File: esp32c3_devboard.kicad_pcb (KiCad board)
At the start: 2 copper layers, 42 parts, among them J1 UART USB, J2 JTAG USB, J3 Conn_01x15_Male, J4 Conn_01x15_Male, SW1 SW_RSTN, SW2 SW_USR, U1 ESP32-C3-MINI-1, U2 SRV05-4, U3 AMS1117, U4 CP2102N-A01-GQFN28

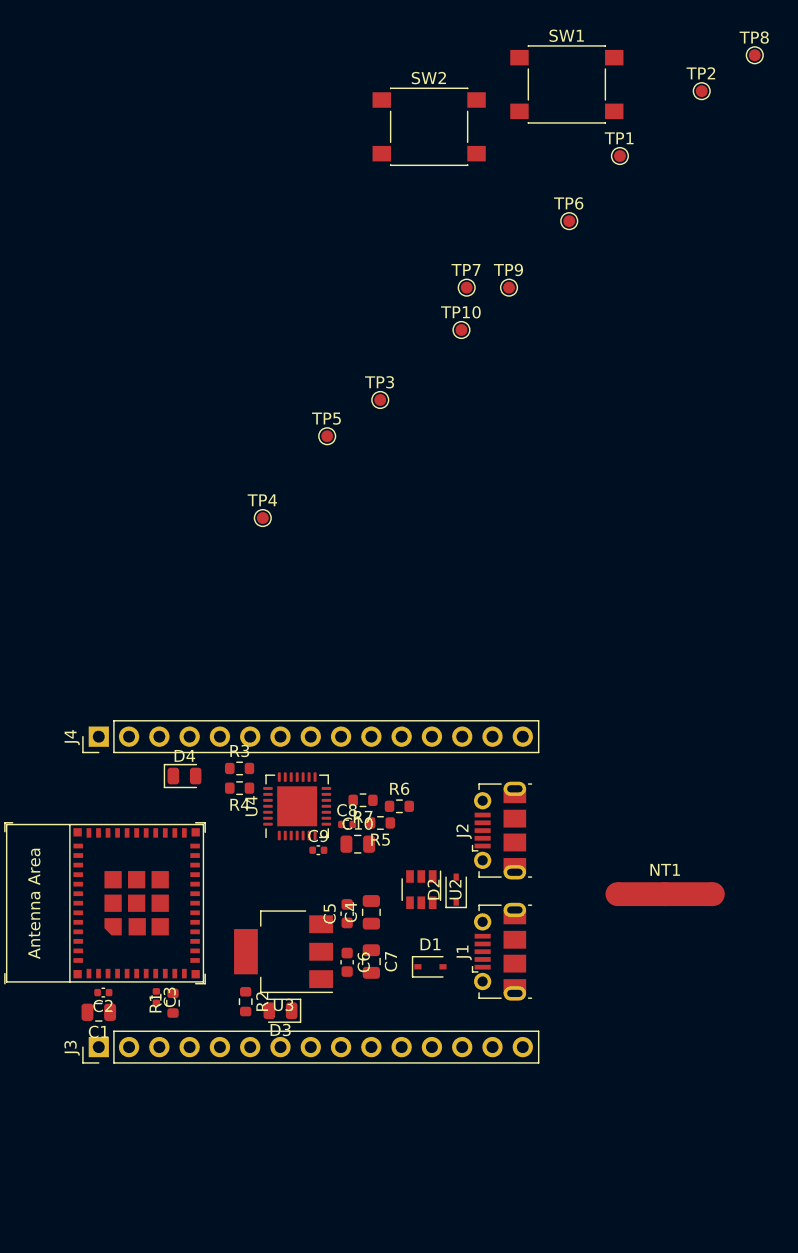
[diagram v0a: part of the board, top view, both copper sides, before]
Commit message: Add pullup on GPIO2 strapping pin
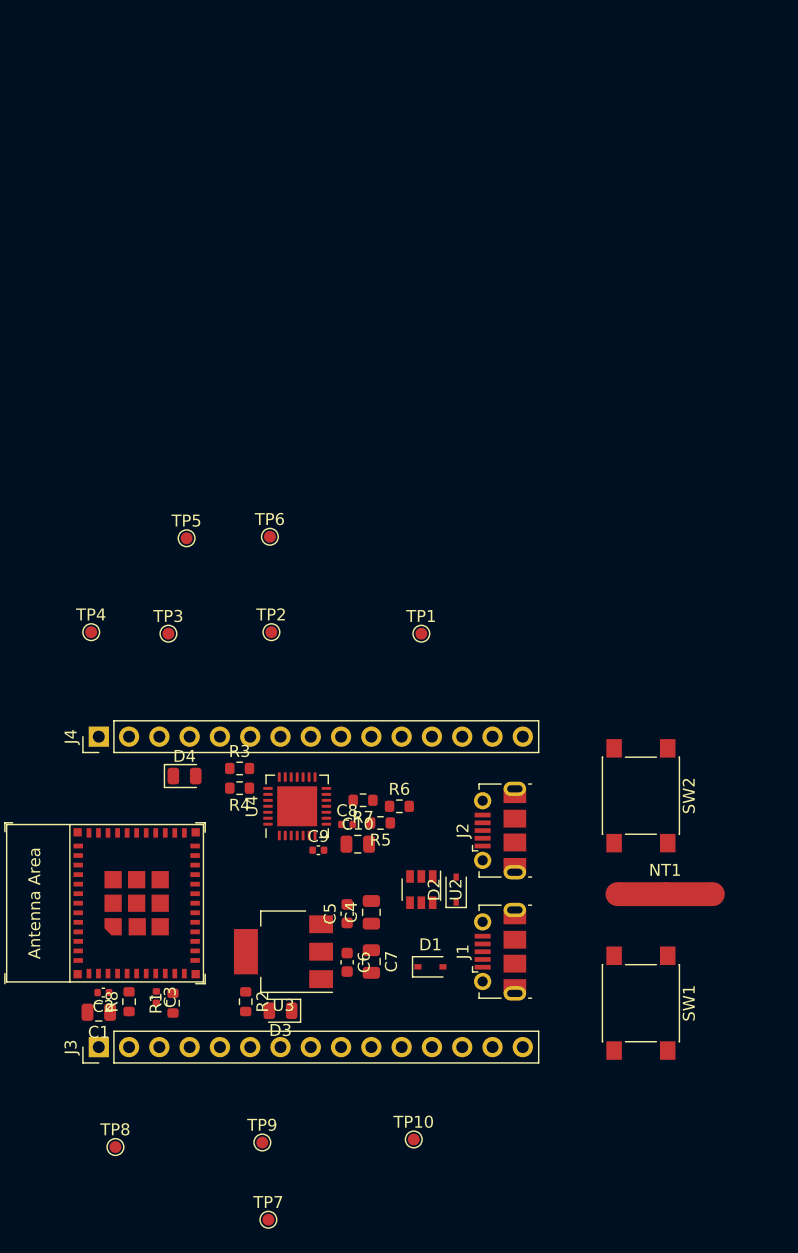
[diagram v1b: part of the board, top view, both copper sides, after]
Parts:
- added R8: 10K, Resistor_SMD:R_0603_1608Metric, F.Cu at (113.0, 149.2)
- moved TP8 106.1 mm to (111.9, 161.4)
- moved TP7 79.9 mm to (124.7, 167.5)
- moved SW1 77.3 mm to (156.0, 149.4), turned to 270 degrees
- moved TP9 74.6 mm to (124.2, 161.0)
- moved TP10 68.0 mm to (136.9, 160.8)
- moved SW2 58.8 mm to (156.0, 132.0), turned to 270 degrees
- moved TP2 58.0 mm to (125.0, 118.2)
- moved TP1 43.4 mm to (137.5, 118.4)
- moved TP6 36.5 mm to (124.8, 110.2)
- moved TP3 26.5 mm to (116.3, 118.4)
- moved TP4 17.3 mm to (109.9, 118.2)
- moved TP5 14.6 mm to (117.9, 110.4)

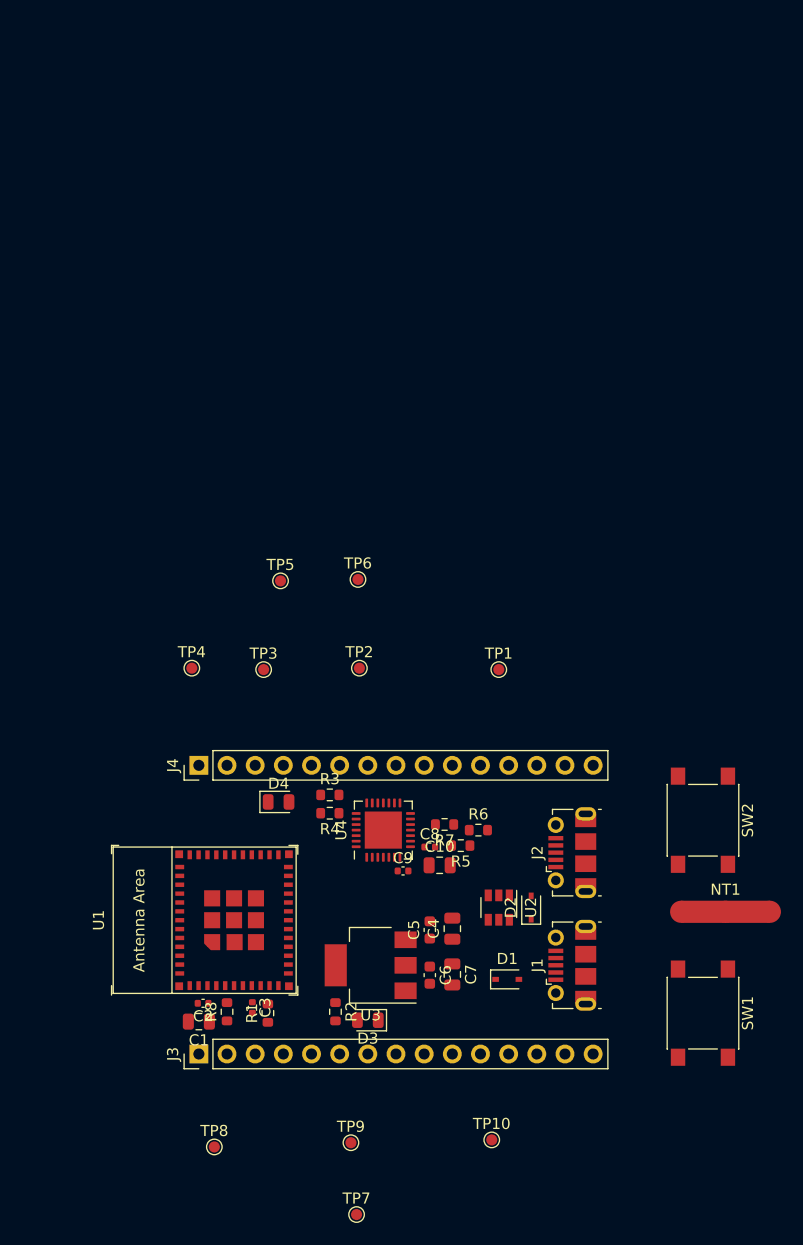
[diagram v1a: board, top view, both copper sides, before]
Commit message: Add micro USB step files
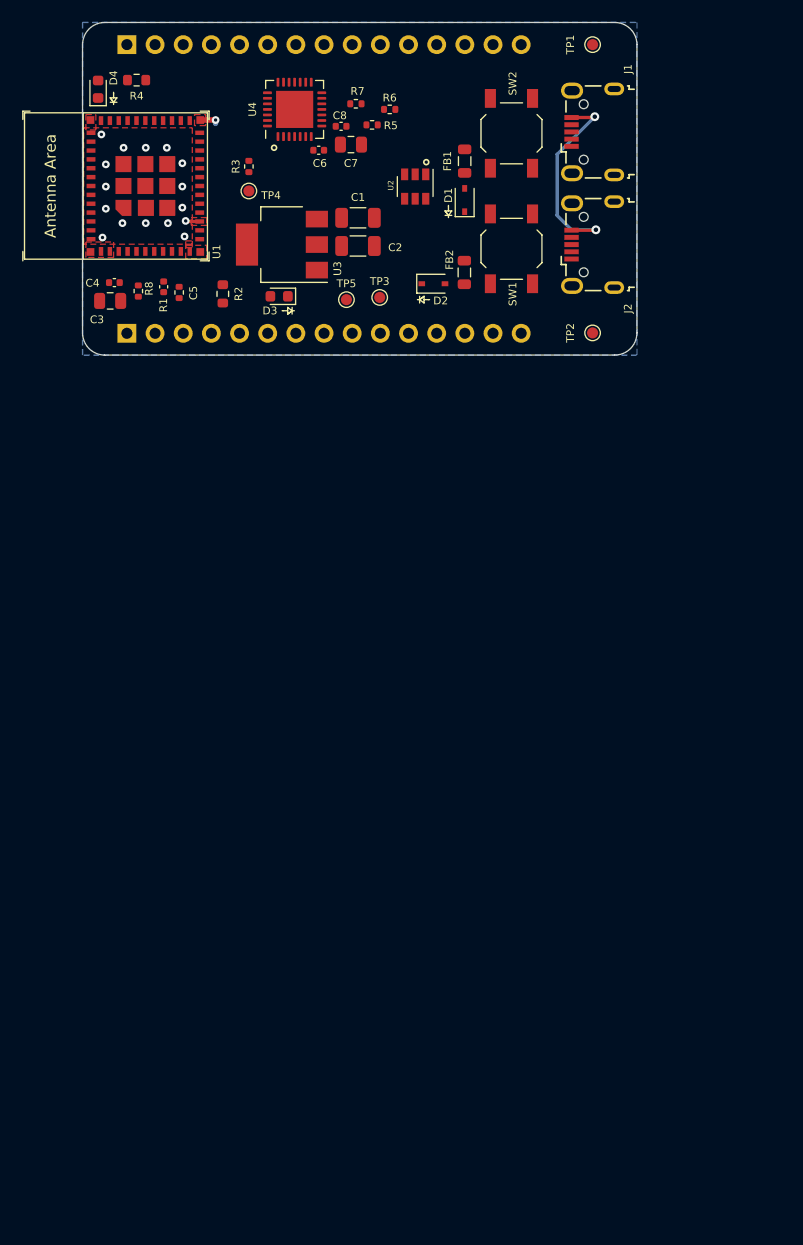
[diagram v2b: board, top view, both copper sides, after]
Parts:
- removed C10: 10uF, Capacitor_SMD:C_0805_2012Metric
- removed the C5 at (131.3, 141.8)
- removed C9: 0.1uF, Capacitor_SMD:C_0402_1005Metric
- removed NT1: Net-Tie_3, NetTie:NetTie-3_SMD_Pad2.0mm
- removed TP10: TP_BOOT_GPIO9, TestPoint:TestPoint_Pad_D1.0mm
- removed TP6: TP_UART_RXD, TestPoint:TestPoint_Pad_D1.0mm
- removed TP7: TP_CHIP_PU, TestPoint:TestPoint_Pad_D1.0mm
- removed TP8: TP_BOOT_GPIO2, TestPoint:TestPoint_Pad_D1.0mm
- removed TP9: TP_BOOT_GPIO8, TestPoint:TestPoint_Pad_D1.0mm
- added C2: 22u, Capacitor_SMD:C_1206_3216Metric, F.Cu at (124.8, 80.2)
- added FB1: 100Ω @ 100MHz, Inductor_SMD:L_0805_2012Metric, F.Cu at (134.5, 72.5)
- added FB2: 100Ω @ 100MHz, Inductor_SMD:L_0805_2012Metric, F.Cu at (134.4, 82.5)
- C1: renamed from C4; value 10uF -> 22u; footprint Capacitor_SMD:C_0805_2012Metric -> Capacitor_SMD:C_1206_3216Metric
- C3: renamed from C1; value 10uF -> 10u
- C4: renamed from C2; value 0.1uF -> 100n
- C6: value 0.1uF -> 100n; footprint Capacitor_SMD:C_0603_1608Metric -> Capacitor_SMD:C_0402_1005Metric
- C7: value 10uF -> 10u
- D3: value RED_LED -> PWR_LED; footprint LED_SMD:LED_0805_2012Metric -> LED_SMD:LED_0603_1608Metric
- D4: value YELLOW_LED -> USR_LED; footprint LED_SMD:LED_0805_2012Metric -> LED_SMD:LED_0603_1608Metric
- J1, J2: footprint Connector_USB:USB_Micro-B_Molex-105017-0001 -> Connector_USB:USB_Micro-B_Wuerth_629105150521
- J3, J4: moved to B.Cu
- R1, R3, R5, R6, R7, R8: footprint Resistor_SMD:R_0603_1608Metric -> Resistor_SMD:R_0402_1005Metric
- R4: value 1.1K -> 470Ω
- SW1: value SW_RSTN -> RSTN_SW; footprint Button_Switch_SMD:SW_Push_1P1T_NO_6x6mm_H9.5mm -> Button_Switch_SMD:SW_SPST_TL3342
- SW2: value SW_USR -> USR_SW; footprint Button_Switch_SMD:SW_Push_1P1T_NO_6x6mm_H9.5mm -> Button_Switch_SMD:SW_SPST_TL3342
- TP5: value TP_UART_TXD -> TP_GND
- U3: value AMS1117 -> AMS1117-3.3
- moved C7 75.4 mm to (124.2, 71.0), turned to 0 degrees
- moved J1 75.2 mm to (146.0, 69.9)
- moved C6 75.1 mm to (121.3, 71.5), turned to 0 degrees
- moved SW1 71.1 mm to (138.7, 80.4)
- moved D1 70.4 mm to (134.5, 76.0), turned to 90 degrees
- moved R4 68.4 mm to (104.9, 65.2)
- moved U1 66.7 mm to (105.7, 74.8)
- moved D4 66.3 mm to (101.4, 66.0), turned to 90 degrees
- moved D3 65.8 mm to (117.7, 84.7)
- moved R2 65.5 mm to (112.7, 84.5)
- moved C8 65.5 mm to (123.3, 69.4)
- moved R6 65.5 mm to (127.7, 67.8)
- moved U4 65.5 mm to (119.1, 67.8)
- moved C3 65.5 mm to (102.5, 85.1)
- moved C4 65.5 mm to (102.9, 83.5)
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- renumbered C3 to C5
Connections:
- net /RED_LED_PU renamed /PWR_LED_A
- net /YELLOW_LED_PU renamed /USR_LED_A
- D1 pad 2: +5VP -> /5V_UART_USB_FLT
- D2 pad 2: +5VL -> /5V_JTAG_USB_FLT
- J1 pad 5: GND1 -> GND
- J2 pad 5: GND2 -> GND
- R5 pad 1: +5VP -> /5V_UART_USB_FLT
- TP5 pad 1: TXD -> GND
- U2 pad 1: JTAG_USB_D- -> UART_USB_D-
- U2 pad 3: JTAG_USB_D+ -> UART_USB_D+
- U2 pad 4: UART_USB_D- -> JTAG_USB_D-
- U2 pad 6: UART_USB_D+ -> JTAG_USB_D+
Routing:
- net GND: track 0.00 -> 21.3 mm, vias 0 -> 19
- added copper zone on B.Cu, net GND
- added copper zone on F.Cu, net GND
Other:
- board outline added: 50 x 30 mm
- net class USB added: clearance 0.2, trace_width 0.25, via_dia 0.8, via_drill 0.4
- rule trace_min: 0.2 -> 0.127
- rule via_min_size: 0.4 -> 0.5

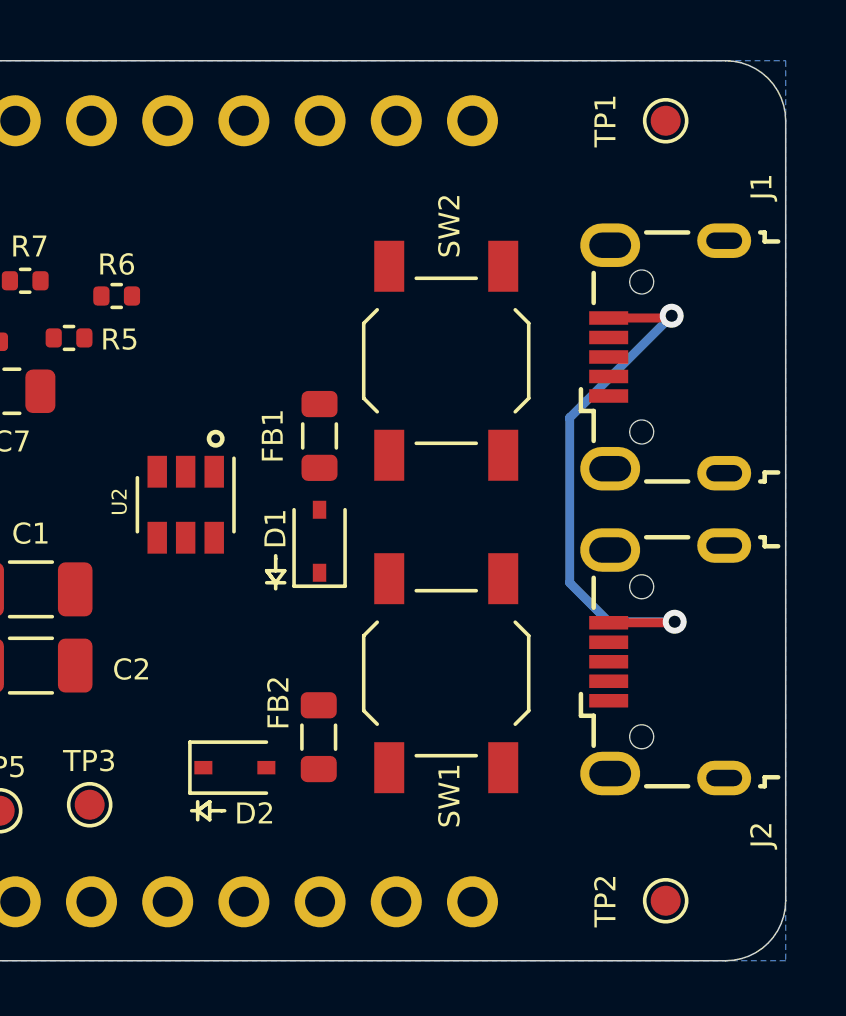
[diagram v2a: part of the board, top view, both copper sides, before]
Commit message: Change button silkscreen labels to RST and BOOT
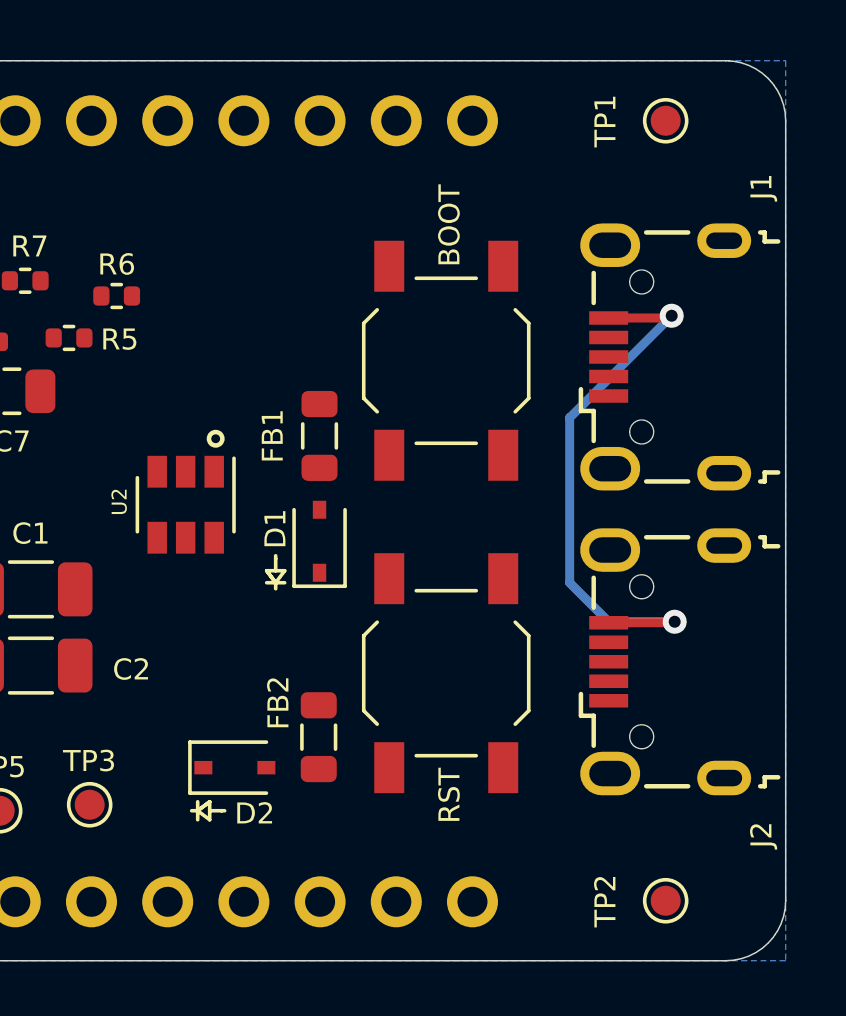
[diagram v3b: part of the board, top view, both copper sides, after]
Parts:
- renumbered SW2 to BOOT, SW1 to RST
